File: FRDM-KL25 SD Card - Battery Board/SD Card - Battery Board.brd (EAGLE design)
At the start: 81.3 x 53.3 mm, 70 parts, among them J10 SSW-103-02-S-S, J11 SSW-102-02-S-S, J12 SSW-103-02-S-S, J13 SSW-103-02-S-S, J14 SSW-103-02-S-S, J15 SSW-103-02-S-S, J16 SSW-103-02-S-S, J17 SSW-103-02-S-S, J18 SSW-103-02-S-S, J19 501568-0207-V2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

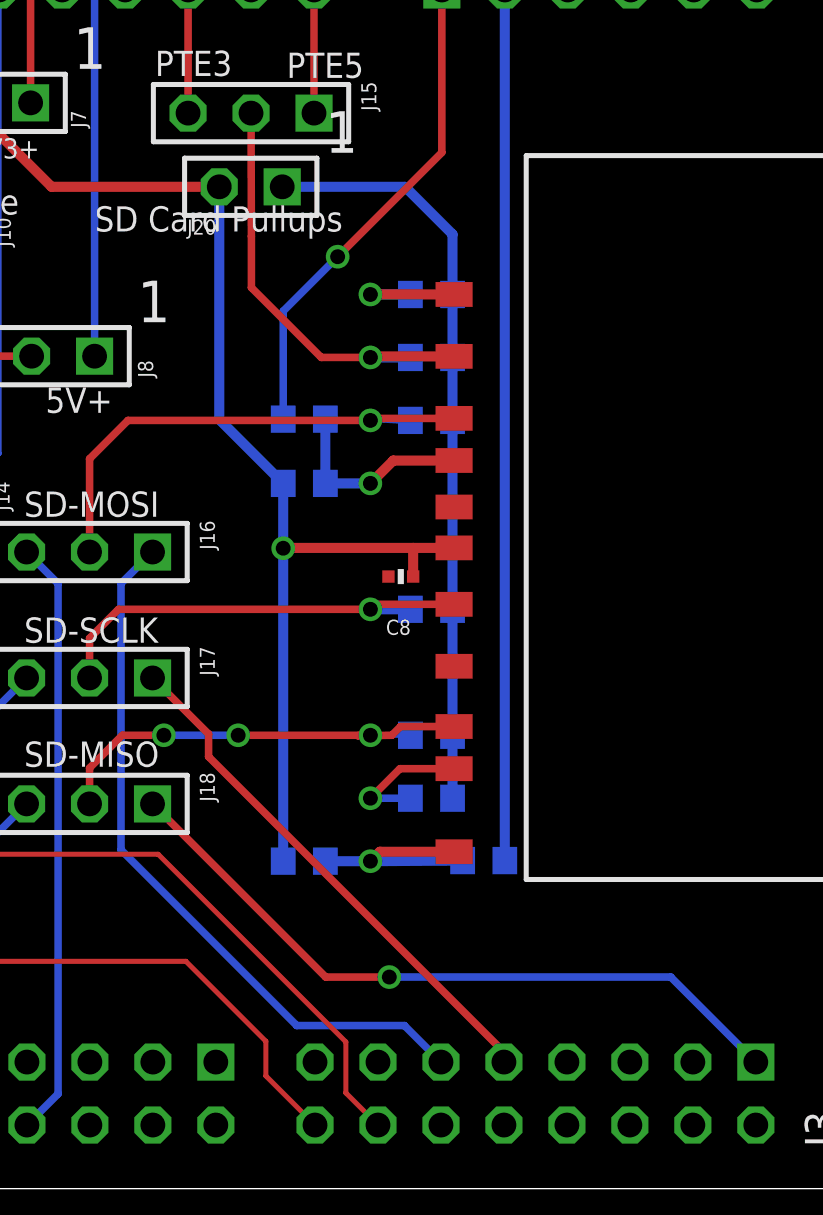
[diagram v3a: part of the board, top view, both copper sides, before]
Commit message: FRDM-KL25Z-I: Some small clean up
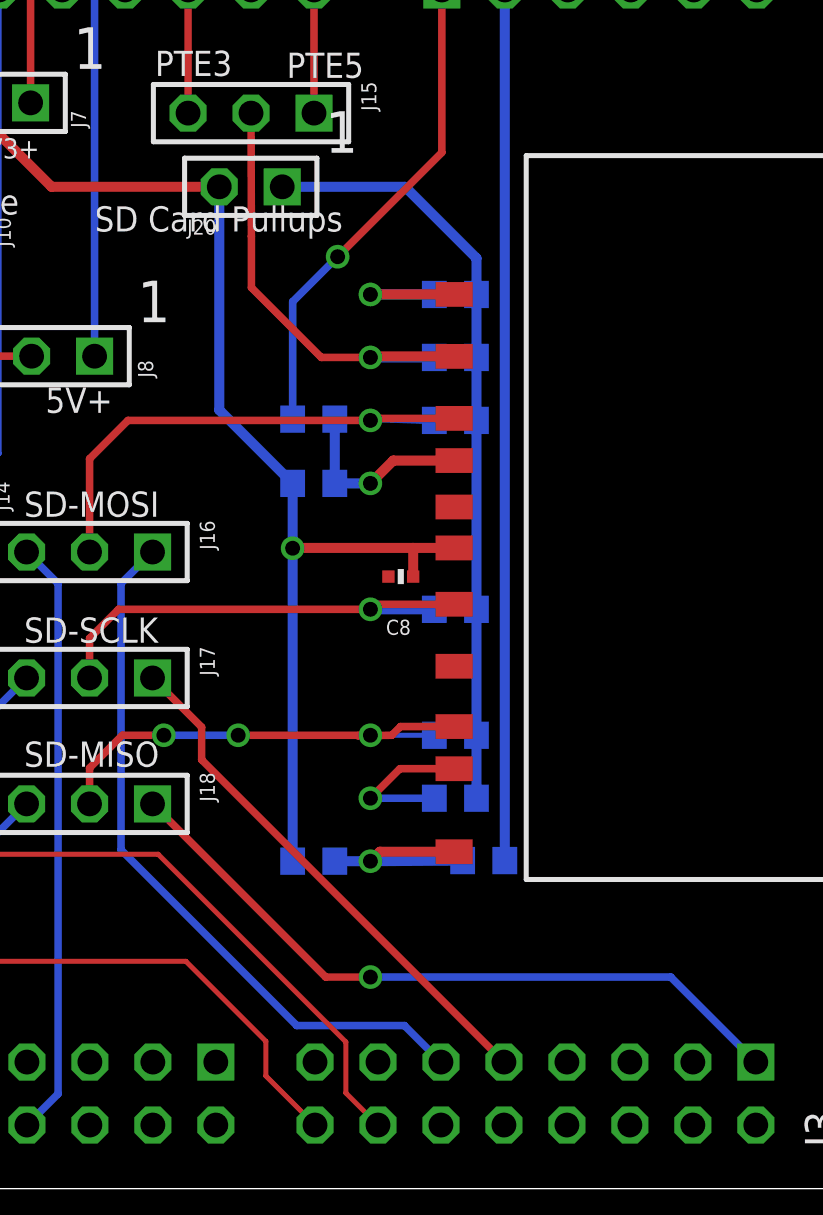
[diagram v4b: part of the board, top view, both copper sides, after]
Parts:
- moved R1 0.97 mm to (36.4, 33.2)
- moved R2 0.97 mm to (36.4, 30.7)
- moved R3 0.97 mm to (36.4, 28.2)
- moved R4 0.97 mm to (36.4, 20.5)
- moved R5 0.97 mm to (36.4, 15.5)
- moved R6 0.97 mm to (36.4, 12.9)
- moved R7 0.38 mm to (30.7, 25.6)
- moved R8 0.38 mm to (30.7, 10.4)
- moved R9 0.38 mm to (30.7, 28.2)
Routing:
- net N$35: track 20.0 -> 20.9 mm
- net N$30: track 18.5 -> 19.5 mm
- net N$25: track 5.48 -> 6.45 mm
- net N$23: track 18.0 -> 19.0 mm
- net N$16: track 4.99 -> 5.96 mm
- net N$27: track 20.8 -> 21.8 mm

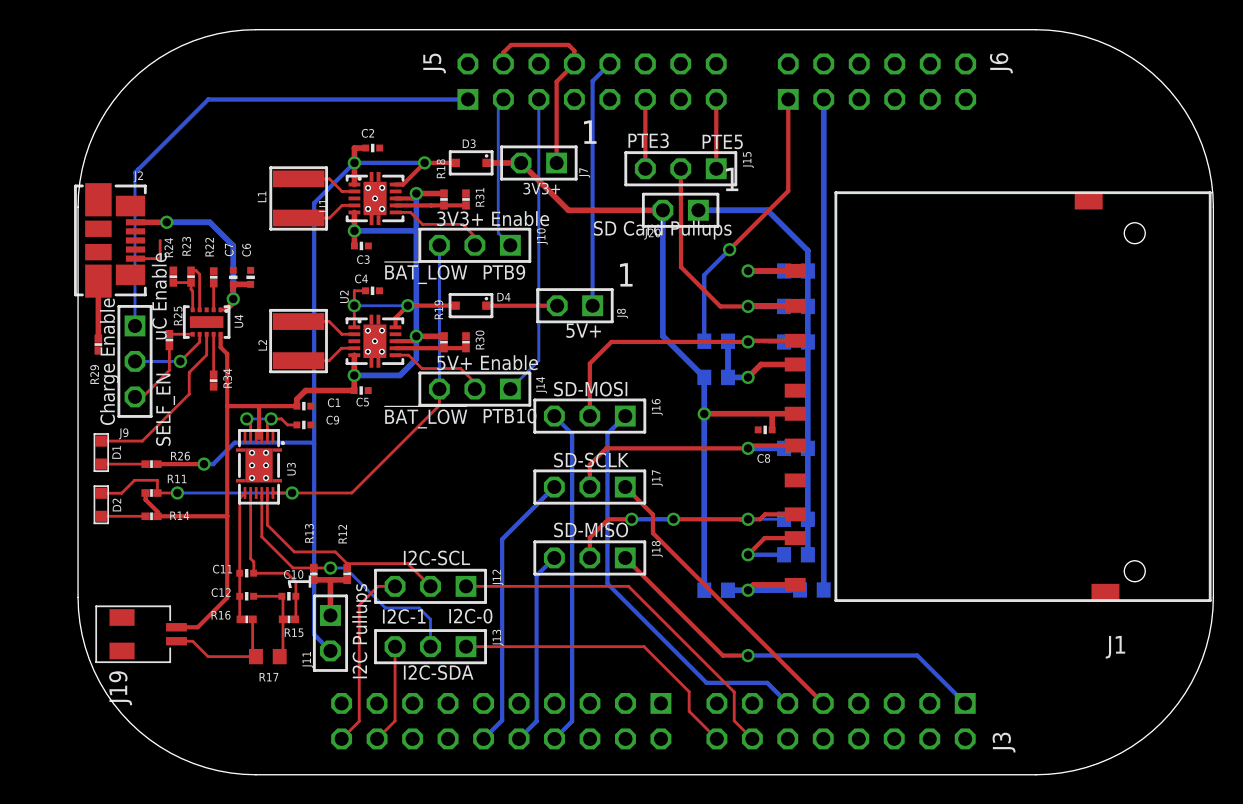
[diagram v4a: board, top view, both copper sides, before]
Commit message: FRDM-KL25Z-I: Cleared all DRU issues except for those that were expected as that is part of the IC design. Also Changed was the boards description from & SD Card Board -> & SD Card Shield
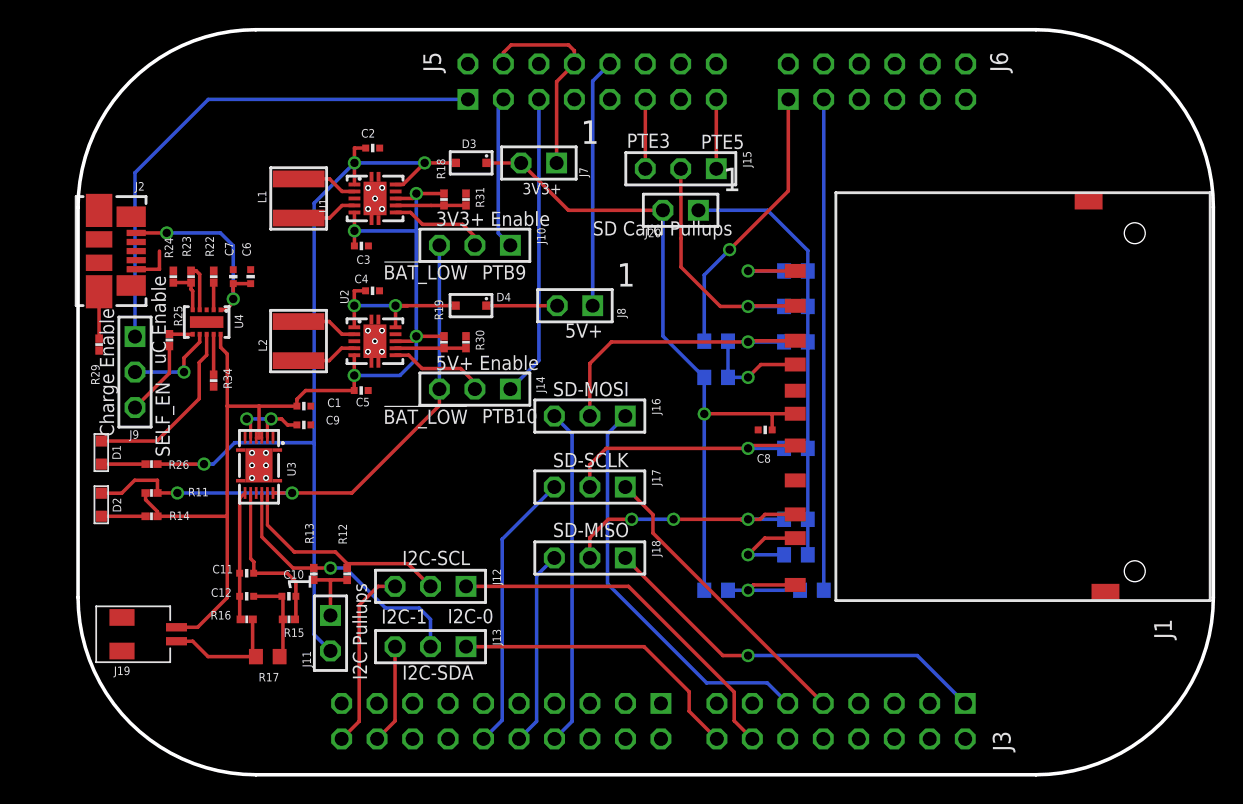
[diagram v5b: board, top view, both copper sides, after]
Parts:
- moved J2 0.76 mm to (-10.8, 34.7)
- moved J9 0.76 mm to (-10.9, 26.0)
- moved R29 0.05 mm to (-13.4, 28.0)
- moved C6 0.05 mm to (-2.59, 32.8)
- moved C7 0.05 mm to (-3.84, 32.8)
- moved R22 0.05 mm to (-5.23, 32.8)
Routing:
- net !FN: track 5.77 -> 6.68 mm
- net UC_EN_CHARGE: track 37.0 -> 37.7 mm
- net N$28: track 4.11 -> 3.35 mm
- net !CHARGE: track 12.5 -> 13.1 mm
- net N$20: track 12.6 -> 13.1 mm
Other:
- board text added: "Kas Lewis KasEmbeddedProjects.blogspot.ca FRDM-KL25Z-I Battery & SD Card Shield 06/2015 Rev A"
- board text removed: "Kas Lewis KasEmbeddedProjects.blogspot.ca FRDM-KL25Z-I Battery & SD Card Board 06/2015 Rev A"

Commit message: FRDM-KL25Z-I: Issue #54 has been resolve din this commit as well as verifying the board is good for seeedstudio. The holes in IC U1, U2 and U3 hav ebeen removed and replaced by a single via as teh fab house does not appear to beable to do this.All part lables have been moved to allow for easy reading and better appearnce
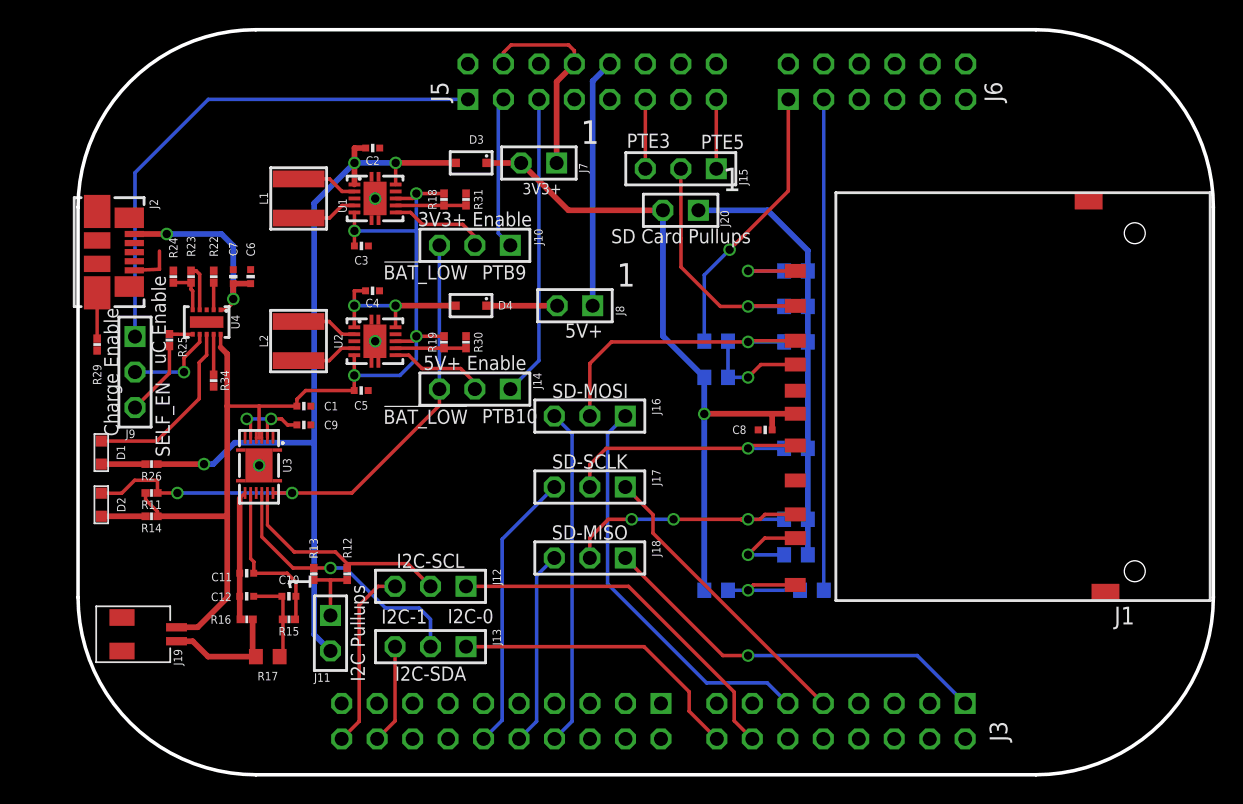
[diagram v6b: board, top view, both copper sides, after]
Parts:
- moved J2 0.16 mm to (-10.9, 34.6)
- moved R29 0.14 mm to (-13.6, 28.0)
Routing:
- net +3V3: track 61.9 -> 60.7 mm

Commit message: FRDM-KL25Z-I: Board almost ready to be sent out, SD Card needs visule check as does J19 (battery connector). The LEDs currently are not making sence as to there footprnt so a physical check will be done with these parts as well
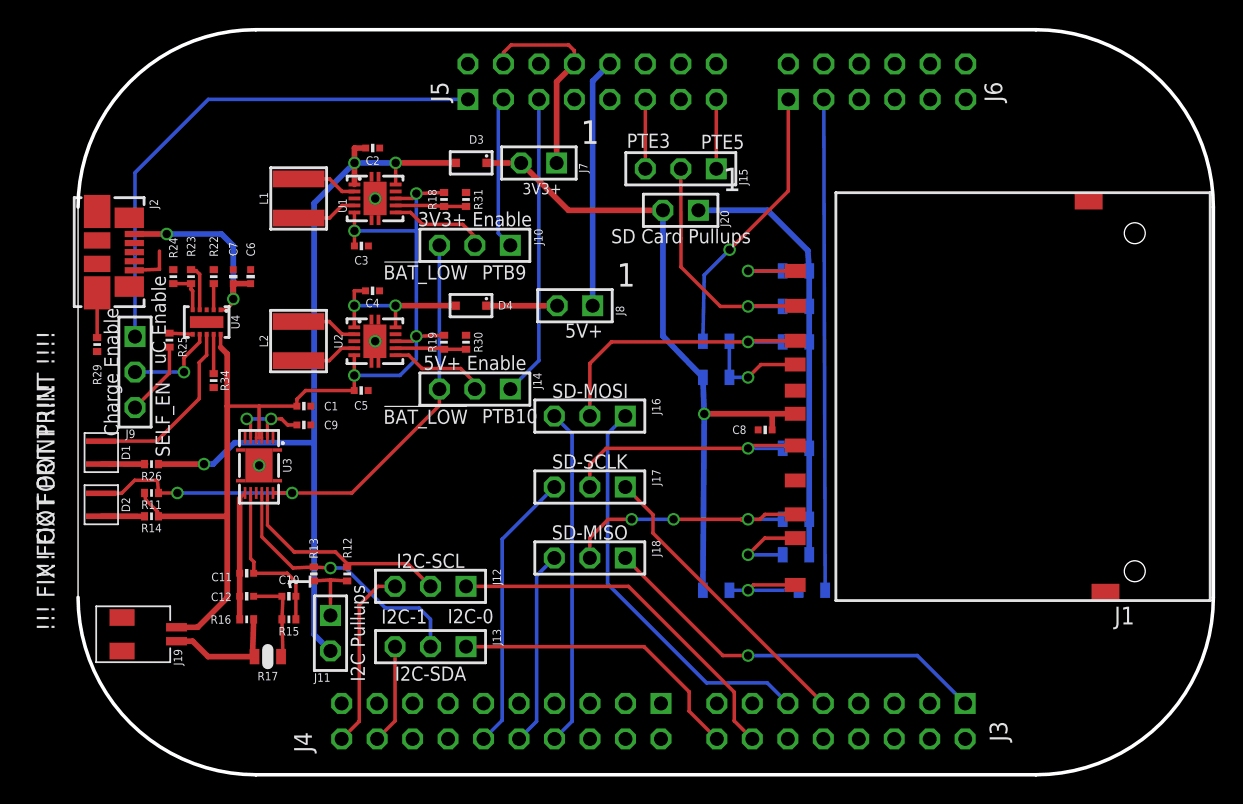
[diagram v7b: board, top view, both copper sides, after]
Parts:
- D1, D2: device Kas-Diodes-LEDs:0.8X1.2 -> Kas-Diodes-LEDs:1.25X1.4

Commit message: FRDM-KL25Z-I: All footprinds have now been verified as outlined in issue #57. with this there was a need to clean up some traces that had been moved by the size of footprints shifting but that has been corrected
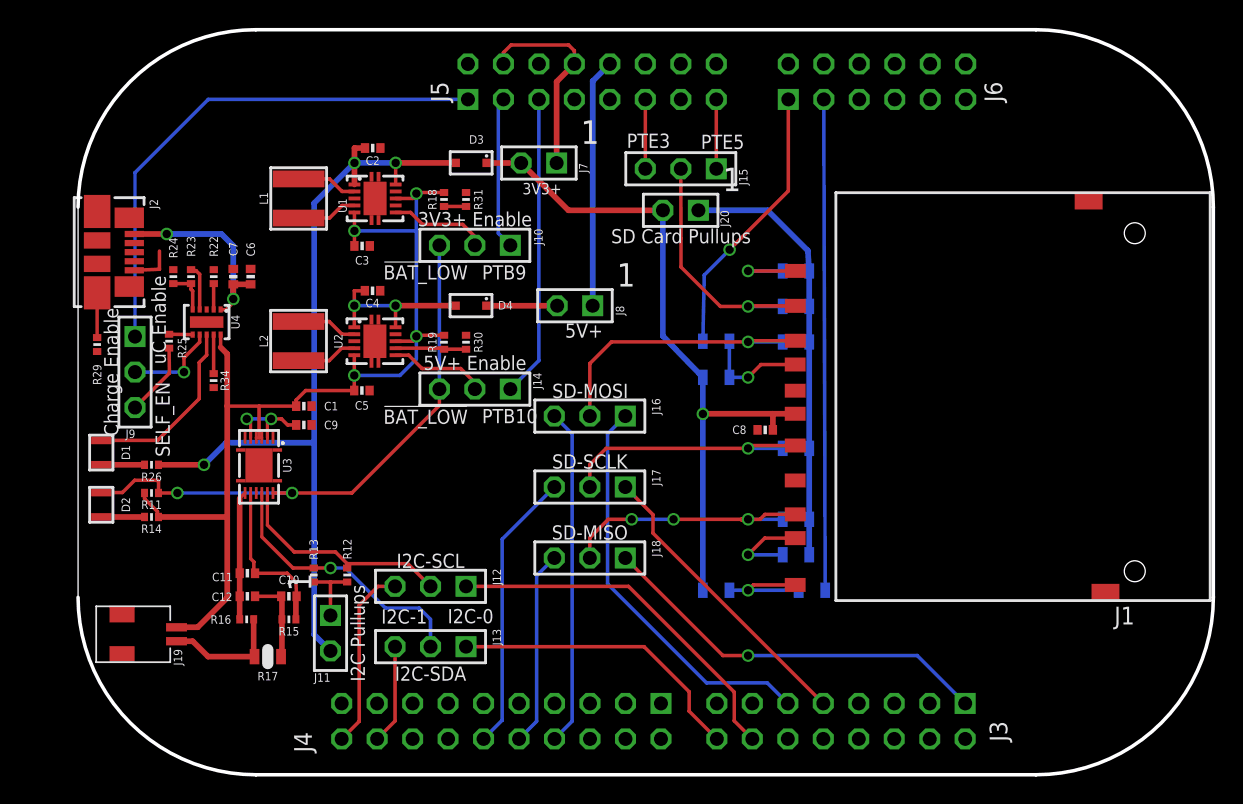
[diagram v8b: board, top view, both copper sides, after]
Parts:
- D1, D2: device Kas-Diodes-LEDs:1.25X1.4 -> Kas-Diodes-LEDs:1.25X2
- moved R25 0.08 mm to (-8.43, 28.2)
- moved R12 0.08 mm to (4.32, 11.5)
- moved R13 0.08 mm to (1.93, 11.5)
- moved C11 0.05 mm to (-2.82, 11.6)
- moved C12 0.05 mm to (-2.82, 9.96)
- moved C3 0.05 mm to (5.39, 35.0)
- moved C5 0.05 mm to (5.37, 24.7)
- moved R14 0.05 mm to (-9.69, 15.6)
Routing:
- net PS/SYNC-1: track 5.04 -> 1.57 mm
